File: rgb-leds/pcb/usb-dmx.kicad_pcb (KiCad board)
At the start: 2 copper layers, 25 x 35 mm, 21 parts, among them J1 USB_C_Receptacle_USB2.0_16P, J2 USB_A, SW1 PTS526_SM15_SMTR2_LFS, U1 IP4234CZ6, U2 ADP2108AUJ-3.3, U3 ESP32-S3-MINI-1U, U4 ST485E

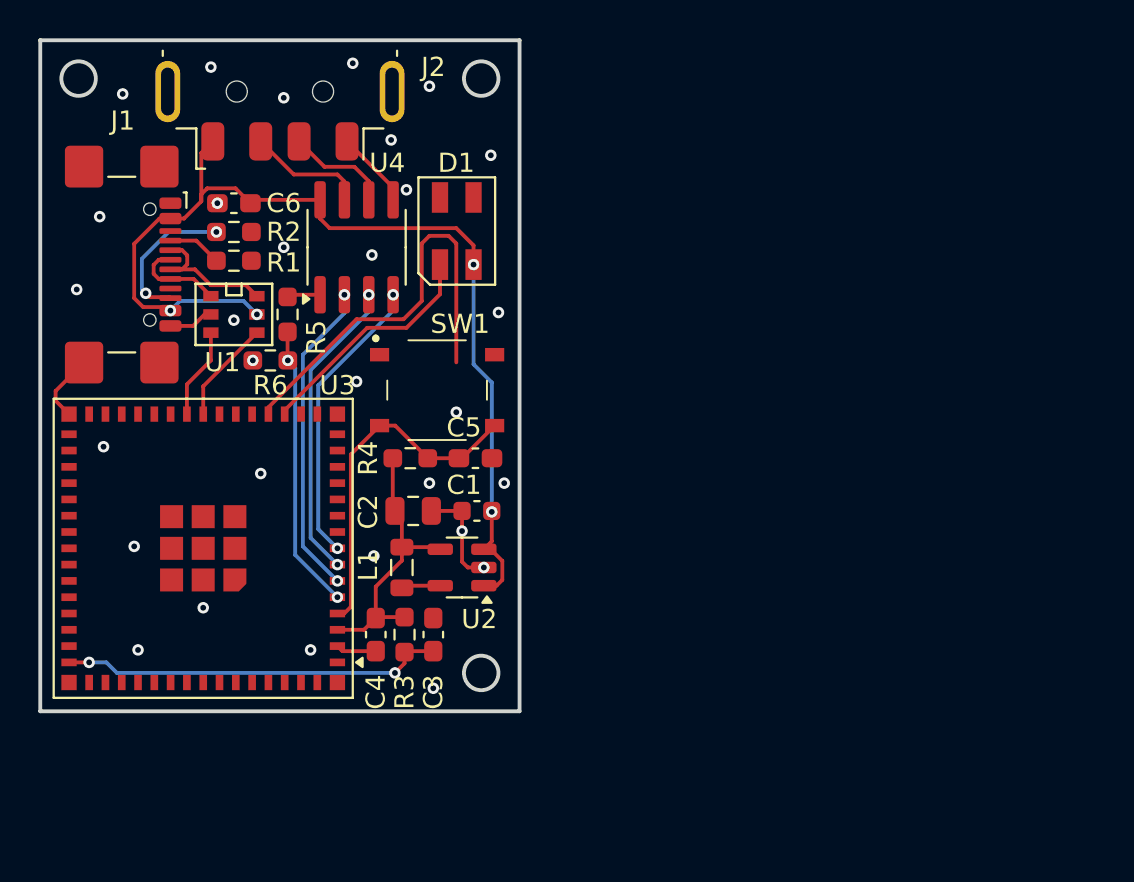
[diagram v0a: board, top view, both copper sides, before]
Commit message: fixing pcb, reorganizing firmware library
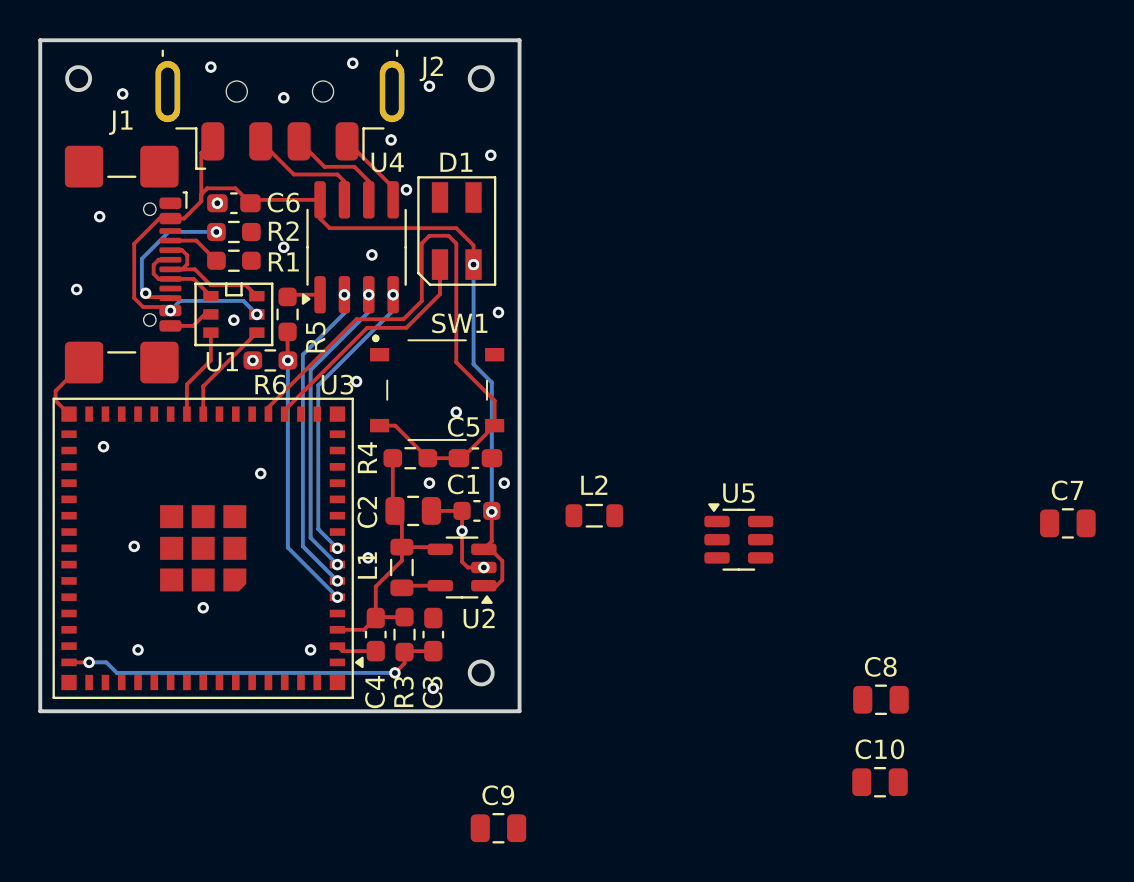
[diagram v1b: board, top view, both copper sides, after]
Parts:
- added C10: 22uF, Capacitor_SMD:C_0805_2012Metric, F.Cu at (131.3, 98.7)
- added C7: 100nF, Capacitor_SMD:C_0805_2012Metric, F.Cu at (141.1, 85.2)
- added C8: 22uF, Capacitor_SMD:C_0805_2012Metric, F.Cu at (131.3, 94.4)
- added C9: 10uF, Capacitor_SMD:C_0805_2012Metric, F.Cu at (111.4, 101.1)
- added L2: 3u9H, Inductor_SMD:L_0805_2012Metric, F.Cu at (116.4, 84.8)
- added U5: AP63203WU, Package_TO_SOT_SMD:TSOT-23-6, F.Cu at (123.9, 86.0)
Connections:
- C5 pad 1: 0 -> 15
- R4 pad 2: 0 -> 15
- SW1 pad 3: 0 -> 15
- SW1 pad 4: 0 -> 15
- U3 pad 4: 0 -> unconnected-(U3-IO0-Pad4)
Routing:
- net 0: track 18.3 -> 0.00 mm
- net 15: track 22.0 -> 33.5 mm
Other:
- outline, holes or cut-outs redrawn
